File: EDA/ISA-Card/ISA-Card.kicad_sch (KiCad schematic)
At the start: 50 parts, among them U7101 74HCT245, U7102 74HCT244, U7104 74HCT138, U7105 74HCT138, U7106 74LS08, U7107 74LS32, U7108 74LS32, U7109 74HC368, U7110 74HC04, U7111 74HC125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

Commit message: clean up schematic
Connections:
- net Port Selection: now reaches U7105.5 (E2), U7107.5, X2.5 (Pin_5), X2.6 (Pin_6), X2.7 (Pin_7), X2.8 (Pin_8)
- net Response: now reaches U7121.11, X5.1 (Pin_1)
- net Command: now reaches U7111.9, U7119.19 (TXD), U7120.9, X5.2 (Pin_2)
- net Data: now reaches U7109.5 (O2a), U7116.14 (SER), U7121.5, X5.3 (Pin_3)
- net Data Clock LV: now reaches U7119.25 (~{RXC}), U7119.9 (~{TXC}), U7121.12, X5.4 (Pin_4)
- net Attention: now reaches U7109.12 (I5), U7109.9 (O4a), U7118.14 (SER), U7119.22 (~{DSR}), U7121.13, X5.5 (Pin_5)
- net Data Clock HV: now reaches U7107.1, U7109.7 (O3a), U7113.11 (C), U7114.6 (Q3), U7116.11 (SRCLK), U7117.11 (SRCLK), U7121.3
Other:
- note added: "300 310 330 340"
- note added: "Clock Generator"
- note added: "Drive Interfacing"
- note added: "ISA Addressing"
- note added: "ISA Data Interface"
- note added: "ISA Port Selection"
- note removed: "PWC"
- moved on the sheet: BUS1, C1, C2, C3, C4, C5, C6, C7, C8, R2, R3, R4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

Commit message: PCB Major Progress
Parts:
- removed C9: C, Capacitor_THT:CP_Radial_D10.0mm_P5.00mm, symbol Device:C
- added C9: C_Polarized, Capacitor_THT:CP_Radial_D10.0mm_P5.00mm, symbol Device:C_Polarized
- C1, C2, C3, C4, C5, C6, C7, C8: footprint Capacitor_SMD:C_0603_1608Metric -> Capacitor_SMD:C_1206_3216Metric
- R1, R10, R11, R12, R13, R14, R15, R16, R2, R3, R4, R5, R6, R7, R8, R9: footprint Resistor_SMD:R_0603_1608Metric -> Resistor_SMD:R_1206_3216Metric
- X2: symbol Connector_Generic:Conn_02x04_Counter_Clockwise -> Connector_Generic:Conn_02x04_Odd_Even
- X5: symbol Connector_Generic:Conn_02x08_Counter_Clockwise -> Connector_Generic:Conn_02x08_Odd_Even
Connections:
- net Attention: now also X5.9 (Pin_9); no longer X5.5 (Pin_5)
- net Command: now also X5.3 (Pin_3); no longer X5.2 (Pin_2)
- net Data: now also X5.5 (Pin_5); no longer X5.3 (Pin_3)
- net Data Clock LV: now also X5.7 (Pin_7); no longer X5.4 (Pin_4)
- net GND: now also U7113.12 (D), X5.2 (Pin_2), X5.4 (Pin_4), C9.2; no longer X5.8 (Pin_8), X5.9 (Pin_9)
- net Port Selection: now also X2.2 (Pin_2), X2.4 (Pin_4); no longer X2.5 (Pin_5), X2.7 (Pin_7)
- net VCC: now also C9.1; no longer U7113.12 (D)
- net at U7104.11 (O4): now also X2.7 (Pin_7); no longer X2.4 (Pin_4)
- net at U7104.12 (O3): now also X2.5 (Pin_5); no longer X2.3 (Pin_3)
- net at U7104.14 (O1): now also X2.3 (Pin_3); no longer X2.2 (Pin_2)
- no-connect marks 23 -> 29
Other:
- moved on the sheet: U7106A, U7107B

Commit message: PCB Primary Routing finished, except 2 traces
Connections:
- net VCC: now also C1.1
- net at C6.2, R2.1, U7110.10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: now also X-TAL1.2; no longer X-TAL1.1
- net at C5.2, R2.2, U7110.11: now also X-TAL1.1; no longer X-TAL1.2
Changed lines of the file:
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@@
   (junction (at 293.37 59.69) (diameter 0) (color 0 0 0 0)
   )
+  (junction (at 55.88 313.69) (diameter 0) (color 0 0 0 0)
+  )
   (junction (at 476.25 114.3) (diameter 0) (color 0 0 0 0)
   )
@@
     (stroke (width 0) (type default) (color 0 0 0 0))
   )
-  (wire (pts (xy 55.88 316.23) (xy 44.45 316.23))
+  (wire (pts (xy 44.45 313.69) (xy 55.88 313.69))
     (stroke (width 0) (type default) (color 0 0 0 0))
   )
@@
     (stroke (width 0) (type default) (color 0 0 0 0))
   )
-  (wire (pts (xy 44.45 316.23) (xy 44.45 322.58))
+  (wire (pts (xy 44.45 313.69) (xy 44.45 322.58))
     (stroke (width 0) (type default) (color 0 0 0 0))
   )
@@
     (pin "1")
   )
-  (symbol (lib_id "Device:Crystal") (at 252.73 29.21 0) (mirror y) (unit 1)
+  (symbol (lib_id "Device:Crystal") (at 252.73 29.21 0) (unit 1)
     (in_bom yes) (on_board yes) (fields_autoplaced)
     (property "Reference" "X-TAL1" (id 0) (at 252.73 21.59 0))
@@
   (symbol (lib_id "power:GND") (at 269.24 176.53 180) (unit 1)
     (in_bom yes) (on_board yes) (fields_autoplaced)
-    (property "Reference" "#PWR?" (id 0) (at 269.24 170.18 0)
+    (property "Reference" "#PWR0144" (id 0) (at 269.24 170.18 0)
       (effects (font (size 1.27 1.27)) hide)
     )
@@
       (reference "#PWR0143") (unit 1) (value "VCC") (footprint "")
     )
+    (path "/c85fd568-008f-409c-98ed-141aeb21416f"
+      (reference "#PWR0144") (unit 1) (value "GND") (footprint "")
+    )
     (path "/08ebbfa7-40a7-4296-9c2e-1cb73819b52e"
       (reference "#PWR0145") (unit 1) (value "GND") (footprint "")
@@
       (reference "#PWR0170") (unit 1) (value "GND") (footprint "")
     )
-    (path "/c85fd568-008f-409c-98ed-141aeb21416f"
-      (reference "#PWR?") (unit 1) (value "GND") (footprint "")
-    )
     (path "/00000000-0000-0000-0000-000077de52a2"

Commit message: update readme
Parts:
- U7119: footprint Package_DIP:DIP-28_W15.24mm_Socket -> Package_DIP:DIP-28_W15.24mm
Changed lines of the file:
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@@
       (effects (font (size 1.524 1.524)))
     )
-    (property "Footprint" "Package_DIP:DIP-28_W15.24mm_Socket" (id 2) (at 391.16 46.99 0)
+    (property "Footprint" "Package_DIP:DIP-28_W15.24mm" (id 2) (at 391.16 46.99 0)
       (effects (font (size 1.524 1.524)) hide)
     )
@@
     )
     (path "/47711afd-a54e-4a94-acca-b81dc67be3e8"
-      (reference "U7119") (unit 1) (value "8251") (footprint "Package_DIP:DIP-28_W15.24mm_Socket")
+      (reference "U7119") (unit 1) (value "8251") (footprint "Package_DIP:DIP-28_W15.24mm")
     )
     (path "/c690bf42-268f-40f6-adde-d54c60b9dc86"

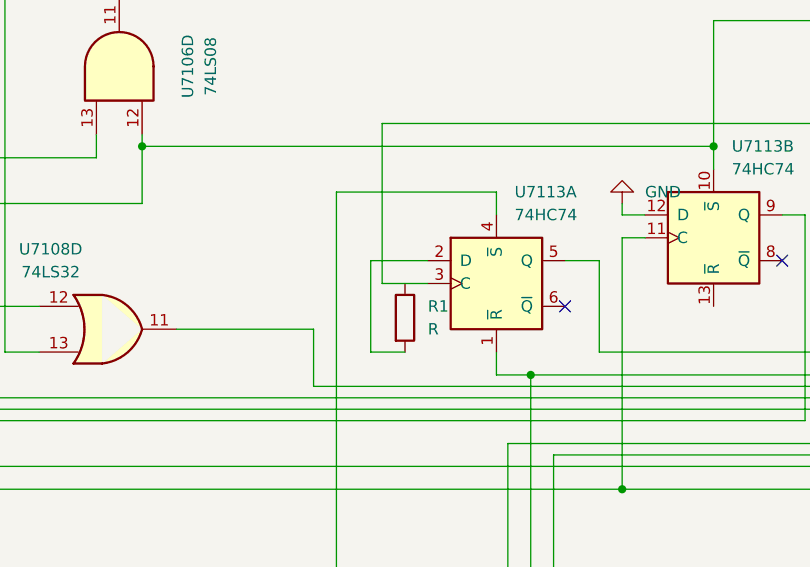
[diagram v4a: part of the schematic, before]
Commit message: Connect RCLKs together and update doc
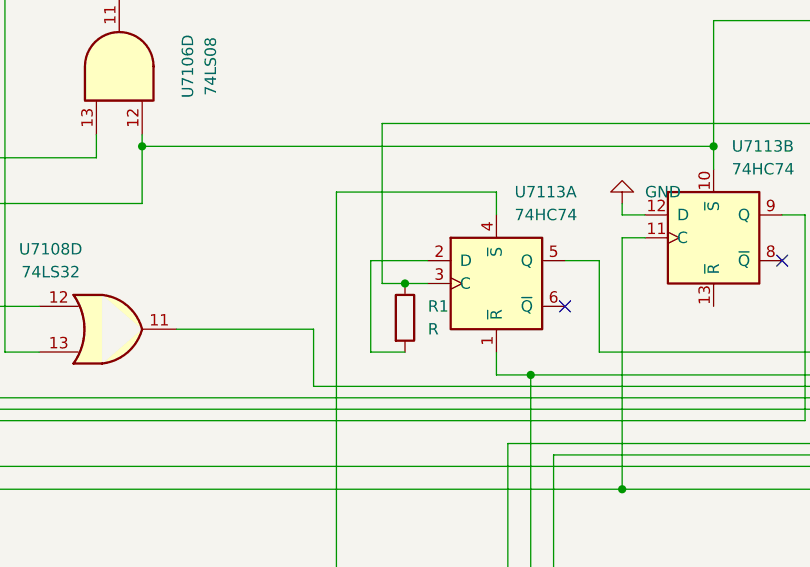
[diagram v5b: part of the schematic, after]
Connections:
- net at U7111.11, U7113.3 (C): now also R1.1
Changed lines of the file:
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@@
   (junction (at 374.65 104.14) (diameter 0) (color 0 0 0 0)
+  )
+  (junction (at 245.11 185.42) (diameter 0) (color 0 0 0 0)
   )
   (junction (at 88.9 411.48) (diameter 0) (color 0 0 0 0)
@@
     (stroke (width 0) (type default) (color 0 0 0 0))
   )
-  (wire (pts (xy 242.57 185.42) (xy 247.65 185.42))
+  (wire (pts (xy 242.57 185.42) (xy 245.11 185.42))
     (stroke (width 0) (type default) (color 0 0 0 0))
   )
@@
     (stroke (width 0) (type default) (color 0 0 0 0))
   )
+  (wire (pts (xy 245.11 185.42) (xy 247.65 185.42))
+    (stroke (width 0) (type default) (color 0 0 0 0))
+  )

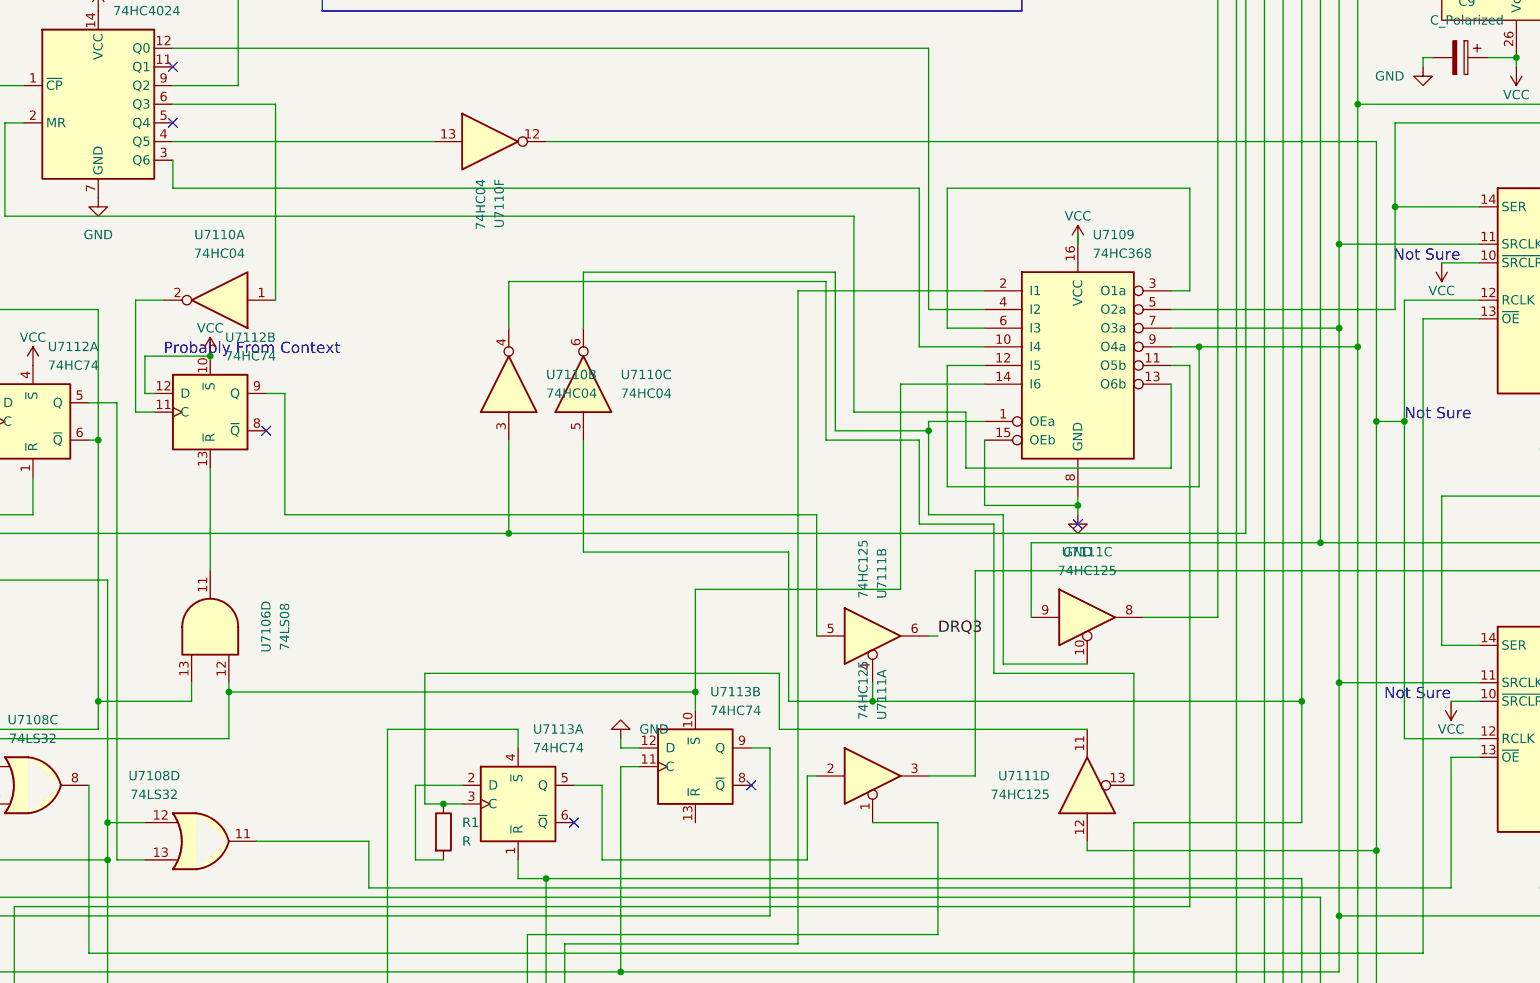
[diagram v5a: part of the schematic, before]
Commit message: Disconnect RCLKs in favor of different idea
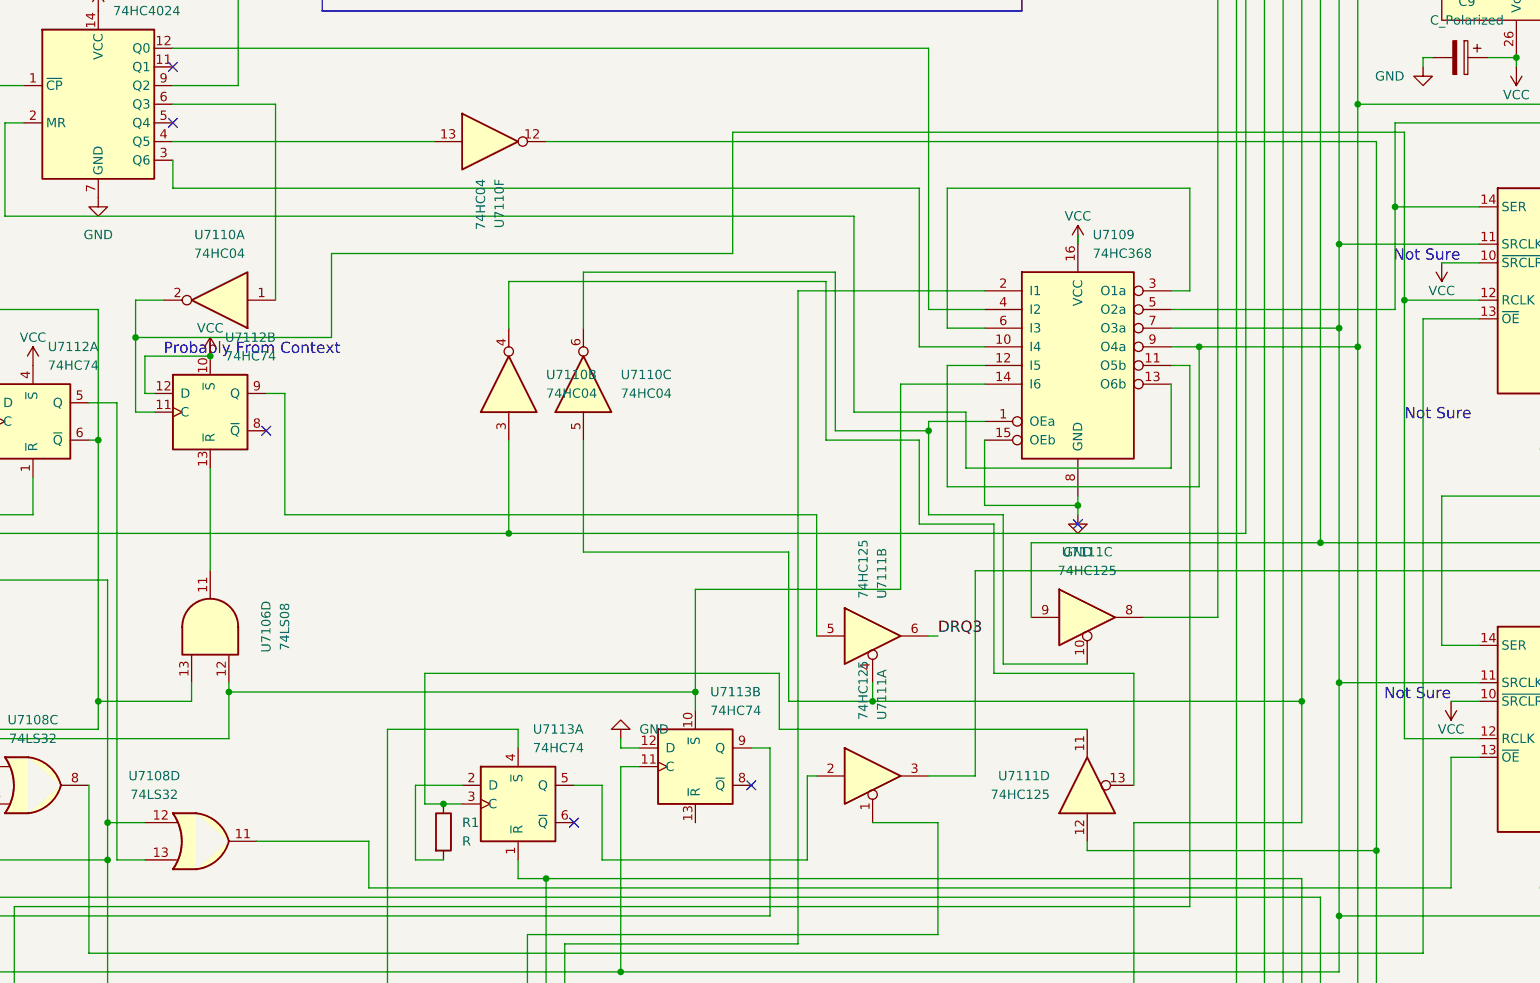
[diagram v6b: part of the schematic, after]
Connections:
- net at U7110.12, U7111.12, U7118.12 (RCLK): no longer U7116.12 (RCLK), U7117.12 (RCLK)
- net at U7110.2, U7112.11 (C): now also U7116.12 (RCLK), U7117.12 (RCLK)
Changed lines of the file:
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@@
   (junction (at 124.46 393.7) (diameter 0) (color 0 0 0 0)
   )
-  (junction (at 375.92 133.35) (diameter 0) (color 0 0 0 0)
-  )
   (junction (at 215.9 170.18) (diameter 0) (color 0 0 0 0)
   )
@@
   (junction (at 320.04 303.53) (diameter 0) (color 0 0 0 0)
   )
-  (junction (at 372.11 133.35) (diameter 0) (color 0 0 0 0)
-  )
   (junction (at 373.38 382.27) (diameter 0) (color 0 0 0 0)
   )
@@
   (junction (at 260.35 39.37) (diameter 0) (color 0 0 0 0)
   )
+  (junction (at 203.2 121.92) (diameter 0) (color 0 0 0 0)
+  )
   (junction (at 367.03 168.91) (diameter 0) (color 0 0 0 0)
   )
@@
   )
   (junction (at 118.11 400.05) (diameter 0) (color 0 0 0 0)
+  )
+  (junction (at 375.92 116.84) (diameter 0) (color 0 0 0 0)
   )
   (junction (at 510.54 78.74) (diameter 0) (color 0 0 0 0)
@@
     (stroke (width 0) (type default) (color 0 0 0 0))
   )
-  (wire (pts (xy 372.11 133.35) (xy 372.11 191.77))
+  (wire (pts (xy 372.11 95.25) (xy 372.11 191.77))
     (stroke (width 0) (type default) (color 0 0 0 0))
   )
@@
     (stroke (width 0) (type default) (color 0 0 0 0))
   )
-  (wire (pts (xy 372.11 133.35) (xy 375.92 133.35))
+  (wire (pts (xy 284.48 110.49) (xy 229.87 110.49))
     (stroke (width 0) (type default) (color 0 0 0 0))
   )
@@
     (stroke (width 0) (type default) (color 0 0 0 0))
   )
-  (wire (pts (xy 375.92 133.35) (xy 375.92 116.84))
+  (wire (pts (xy 375.92 116.84) (xy 375.92 176.53))
     (stroke (width 0) (type default) (color 0 0 0 0))
   )
@@
     (stroke (width 0) (type default) (color 0 0 0 0))
   )
+  (wire (pts (xy 375.92 93.98) (xy 284.48 93.98))
+    (stroke (width 0) (type default) (color 0 0 0 0))
+  )
   (wire (pts (xy 267.97 311.15) (xy 267.97 313.69))
     (stroke (width 0) (type default) (color 0 0 0 0))
@@
     (stroke (width 0) (type default) (color 0 0 0 0))
   )
+  (wire (pts (xy 375.92 116.84) (xy 375.92 93.98))
+    (stroke (width 0) (type default) (color 0 0 0 0))
+  )
   (wire (pts (xy 43.18 69.85) (xy 33.02 69.85))
     (stroke (width 0) (type default) (color 0 0 0 0))
@@
     (stroke (width 0) (type default) (color 0 0 0 0))
   )
+  (wire (pts (xy 229.87 121.92) (xy 203.2 121.92))
+    (stroke (width 0) (type default) (color 0 0 0 0))
+  )
   (wire (pts (xy 367.03 208.28) (xy 367.03 200.66))
     (stroke (width 0) (type default) (color 0 0 0 0))
@@
     (stroke (width 0) (type default) (color 0 0 0 0))
   )
+  (wire (pts (xy 229.87 110.49) (xy 229.87 121.92))
+    (stroke (width 0) (type default) (color 0 0 0 0))
+  )
   (wire (pts (xy 260.35 29.21) (xy 260.35 39.37))
     (stroke (width 0) (type default) (color 0 0 0 0))
@@
     (stroke (width 0) (type default) (color 0 0 0 0))
   )
-  (wire (pts (xy 372.11 95.25) (xy 372.11 133.35))
-    (stroke (width 0) (type default) (color 0 0 0 0))
-  )
   (wire (pts (xy 199.39 193.04) (xy 181.61 193.04))
     (stroke (width 0) (type default) (color 0 0 0 0))
@@
     (stroke (width 0) (type default) (color 0 0 0 0))
   )
-  (wire (pts (xy 375.92 176.53) (xy 375.92 133.35))
-    (stroke (width 0) (type default) (color 0 0 0 0))
-  )
   (wire (pts (xy 359.41 17.78) (xy 359.41 288.29))
     (stroke (width 0) (type default) (color 0 0 0 0))
@@
     (stroke (width 0) (type default) (color 0 0 0 0))
   )
+  (wire (pts (xy 203.2 121.92) (xy 203.2 132.08))
+    (stroke (width 0) (type default) (color 0 0 0 0))
+  )
   (wire (pts (xy 406.4 49.53) (xy 416.56 49.53))
     (stroke (width 0) (type default) (color 0 0 0 0))
@@
     (stroke (width 0) (type default) (color 0 0 0 0))
   )
-  (wire (pts (xy 203.2 116.84) (xy 203.2 132.08))
+  (wire (pts (xy 203.2 116.84) (xy 203.2 121.92))
     (stroke (width 0) (type default) (color 0 0 0 0))
   )
@@
     (stroke (width 0) (type default) (color 0 0 0 0))
   )
+  (wire (pts (xy 284.48 93.98) (xy 284.48 110.49))
+    (stroke (width 0) (type default) (color 0 0 0 0))
+  )

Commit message: cleanup
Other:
- company: Designed by Sergey Kiselev -> Shelby Jueden (Tech Tangents)
- title: Monster Floppy Disk Controller -> Philips CM-153 LMSI Reproduction Card
